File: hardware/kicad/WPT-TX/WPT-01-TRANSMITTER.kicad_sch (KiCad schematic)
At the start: 8 parts, among them J2 Conn_01x12_Pin, J3 Conn_01x05_Pin, J4 Conn_01x04_Pin, J5 12401610E4#2A, SW1 EC11E09244AQ

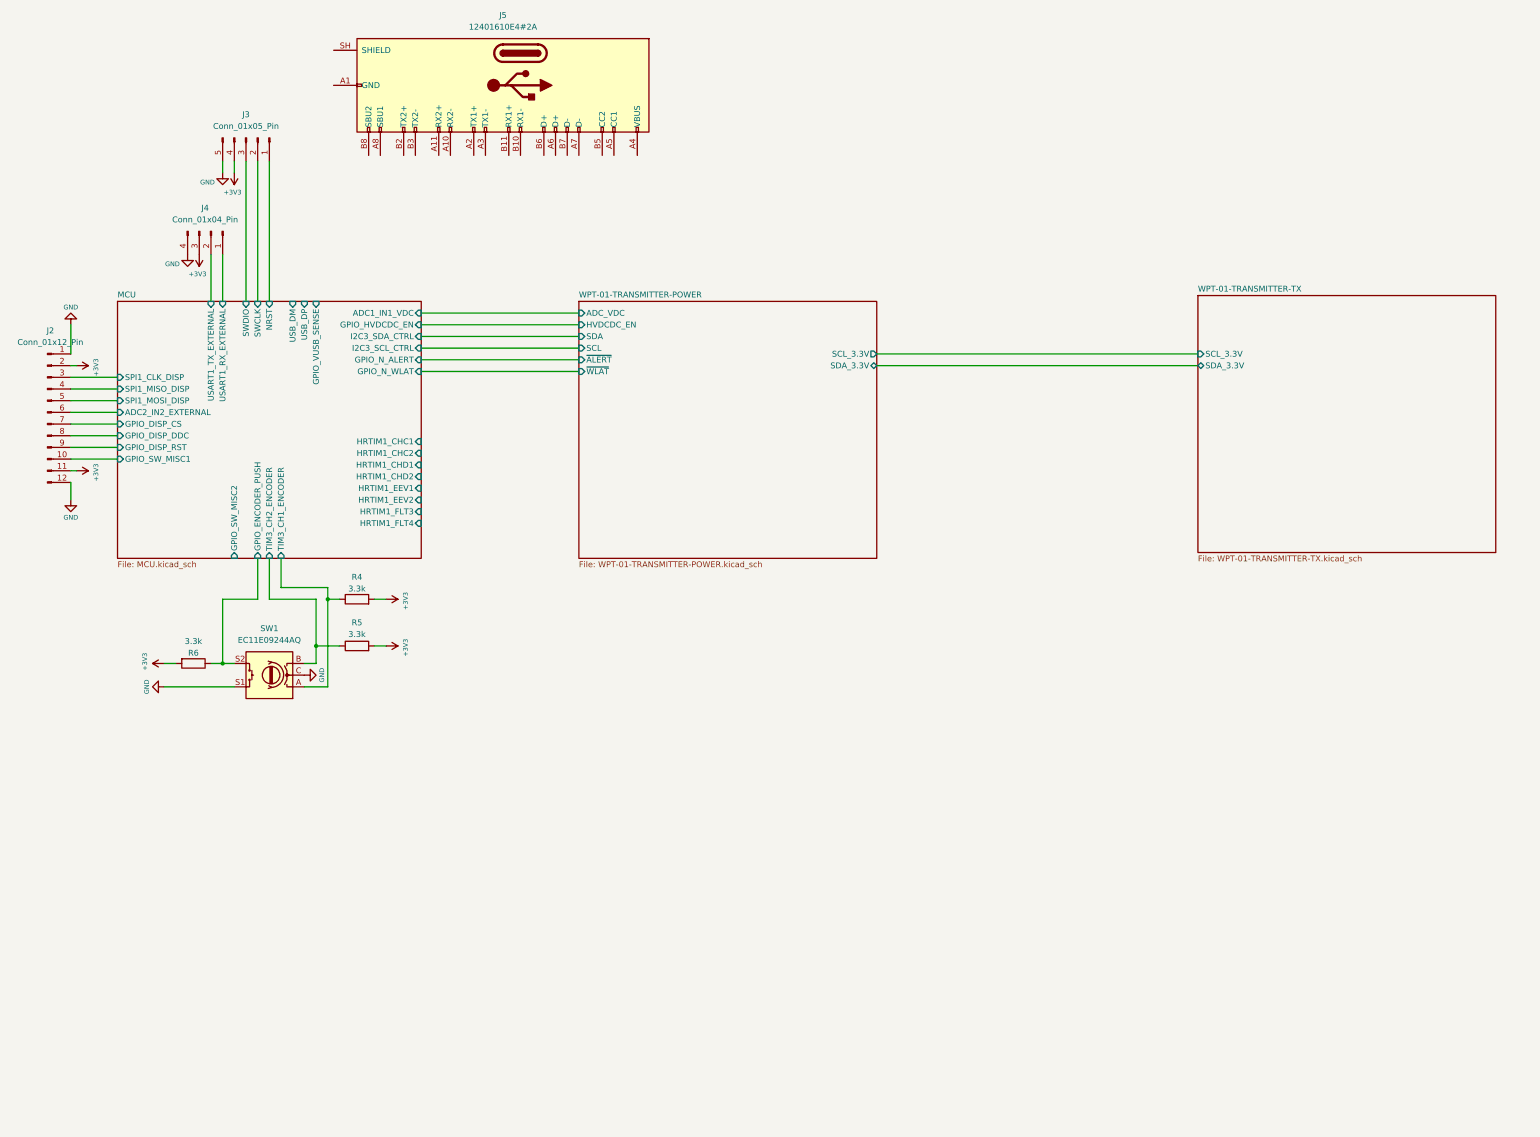
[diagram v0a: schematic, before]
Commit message: add voltage divider for vbus
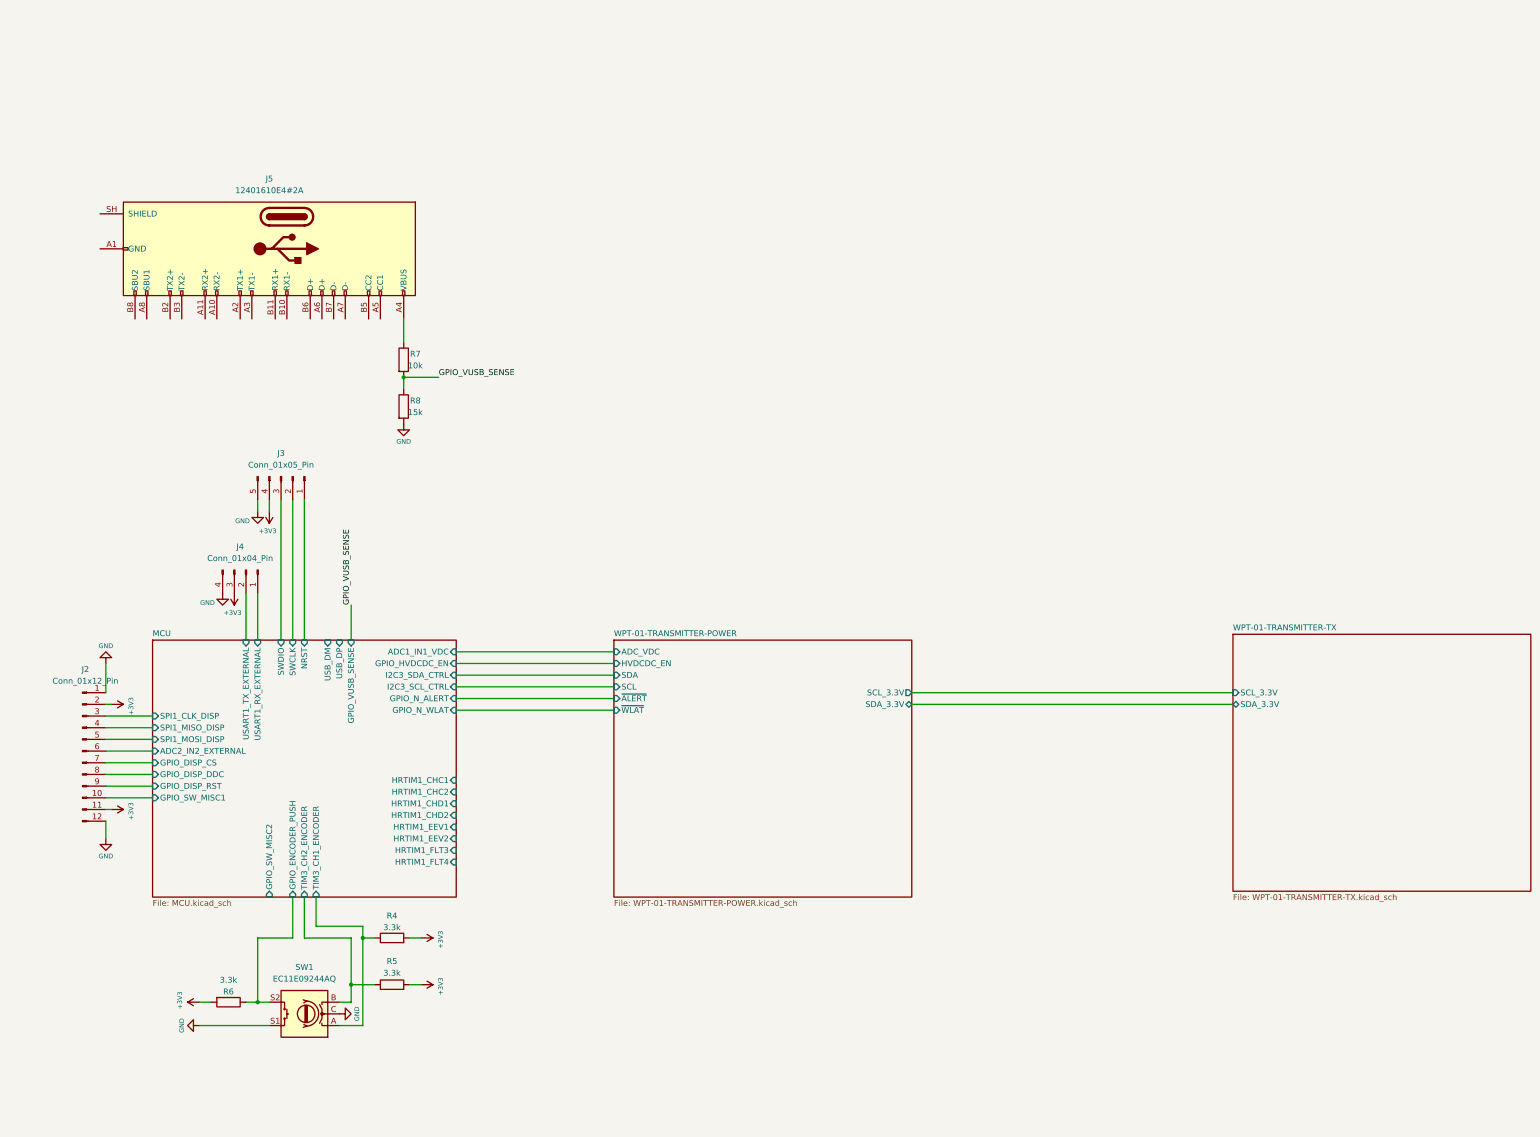
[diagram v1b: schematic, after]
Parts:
- added R7: 10k, Resistor_SMD:R_0402_1005Metric, symbol Device:R
- added R8: 15k, Resistor_SMD:R_0402_1005Metric, symbol Device:R
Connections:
- net GND: now also R8.2
- net at J5.A4 (VBUS), J5.A9 (VBUS), J5.B4 (VBUS)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: now also R7.1
- new net GPIO_VUSB_SENSE: R7.2, R8.1
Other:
- moved on the sheet: J2, J3, J4, J5, R4, R5, R6, SW1

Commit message: USB−C routing
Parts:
- added R10, R9: 5.1k, Resistor_SMD:R_0402_1005Metric, symbol Device:R
- added U3: USBLC6-2SC6, Package_TO_SOT_SMD:SOT-23-6, symbol Power_Protection:USBLC6-2SC6
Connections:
- net GND: now also J5.A1 (GND), J5.A12 (GND), J5.B1 (GND), J5.B12 (GND), J5.SH (SHIELD), R10.2, R9.2, U3.2 (GND)
- net VBUS: now reaches J5.A4 (VBUS), J5.A9 (VBUS), J5.B4 (VBUS), J5.B9 (VBUS), R7.1
- net VBUS: now also U3.5 (VBUS)
- net at J5.A5 (CC1): now also R9.1
- net USB_DP: now reaches J5.A6 (D+)
- net USB_DP: now also J5.B6 (D+), U3.1 (I/O1), U3.6 (I/O1)
- net USB_DM: now reaches J5.A7 (D-)
- net USB_DM: now also J5.B7 (D-), U3.3 (I/O2), U3.4 (I/O2)
- net at J5.B5 (CC2): now also R10.1
- no-connect marks 0 -> 10

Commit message: USB + interlock
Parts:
- added R11: 0, Resistor_SMD:R_0402_1005Metric, symbol Device:R
- added SW2: EG2219, Button_Switch_THT:SW_E-Switch_EG2219_DPDT_Angled, symbol Switch:SW_DPDT_x2
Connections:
- net +3V3: now also SW2.4 (A)
- net GND: now also SW2.6 (C)
- new net HV_EN_MCU: R11.2, SW2.1 (A)
- new net HV_EN_SW: R11.1, SW2.2 (B)
- new net HV_SW_STATE: SW2.5 (B)
- no-connect marks 10 -> 11

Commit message: HRTIM
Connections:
- net MCU/ADC2_IN2_EXTERNAL renamed MCU/ADC2_IN8_EXTERNAL
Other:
- sheet MCU ports: added ADC2_IN8_EXTERNAL, VSWA_CMP, VSWB_CMP; removed ADC2_IN2_EXTERNAL
- sheet WPT-01-TRANSMITTER-TX ports: added HRTIM1_CHC1, HRTIM1_CHC2, HRTIM1_CHD1, HRTIM1_CHD2, HRTIM1_EEV1, HRTIM1_EEV2, HRTIM1_FLT3, HRTIM1_FLT4, VSWA_CMP, VSWB_CMP; removed none
- moved on the sheet: R11, SW2A, SW2B

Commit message: sch: USB4105, standard headers, drop R_LEG
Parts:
- J2: footprint (none) -> Connector_PinHeader_2.54mm:PinHeader_1x12_P2.54mm_Vertical
- J3: footprint (none) -> Connector_PinHeader_2.54mm:PinHeader_1x05_P2.54mm_Vertical
- J4: footprint (none) -> Connector_PinHeader_2.54mm:PinHeader_1x04_P2.54mm_Vertical
- J5: value 12401610E4#2A -> USB4105-GF-A; footprint Connector_USB:USB_C_Receptacle_Amphenol_12401610E4-2A -> Connector_USB:USB_C_Receptacle_GCT_USB4105-xx-A_16P_TopMnt_Horizontal; symbol Connector:USB_C_Receptacle -> Connector:USB_C_Receptacle_USB2.0_16P
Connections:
- no-connect marks 11 -> 3
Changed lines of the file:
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@@
 			)
 		)
-		(property "Footprint" ""
+		(property "Footprint" "Connector_PinHeader_2.54mm:PinHeader_1x05_P2.54mm_Vertical"
 			(at 96.52 111.76 0)
 			(hide yes)
@@
 			)
 		)
-		(property "Footprint" ""
+		(property "Footprint" "Connector_PinHeader_2.54mm:PinHeader_1x04_P2.54mm_Vertical"
 			(at 88.9 132.08 0)
 			(hide yes)
@@
 	)
 	(symbol
-		(lib_id "Connector:USB_C_Receptacle")
-		(at 97.79 62.23 270)
+		(lib_id "Connector:USB_C_Receptacle_USB2.0_16P")
+		(at 107.95 62.23 270)
 		(unit 1)
 		(body_style 1)
@@
 		(in_pos_files yes)
 		(dnp no)
-		(fields_autoplaced yes)
 		(property "Reference" "J5"
-			(at 93.98 46.99 90)
+			(at 107.95 46.99 90)
 			(show_name no)
 			(do_not_autoplace no)
@@
 			)
 		)
-		(property "Value" "12401610E4#2A"
-			(at 93.98 49.53 90)
+		(property "Value" "USB4105-GF-A"
+			(at 107.95 49.53 90)
 			(show_name no)
 			(do_not_autoplace no)
@@
 			)
 		)
-		(property "Footprint" "Connector_USB:USB_C_Receptacle_Amphenol_12401610E4-2A"
-			(at 97.79 66.04 0)
+		(property "Footprint" "Connector_USB:USB_C_Receptacle_GCT_USB4105-xx-A_16P_TopMnt_Horizontal"
+			(at 107.95 62.23 0)
 			(hide yes)
 			(show_name no)
@@
 			)
 		)
-		(property "Datasheet" "https://www.usb.org/sites/default/files/documents/usb_type-c.zip"
-			(at 97.79 66.04 0)
+		(property "Datasheet" "https://gct.co/files/drawings/usb4105.pdf"
+			(at 107.95 62.23 0)
 			(hide yes)
 			(show_name no)
@@
 			)
 		)
-		(property "Description" "USB Full-Featured Type-C Receptacle connector"
-			(at 97.79 62.23 0)
+		(property "Description" "USB 2.0-only Type-C Receptacle connector, 16 pin (GCT USB4105)"
+			(at 107.95 62.23 0)
 			(hide yes)
 			(show_name no)
@@
 			)
 		)
-		(pin "A12"
-		)
-		(pin "B1"
+		(pin "A1"
 		)
-		(pin "B2"
+		(pin "A4"
 		)
-		(pin "A10"
+		(pin "A5"
 		)
-		(pin "A11"
+		(pin "A6"
 		)
 		(pin "A7"
@@
 		(pin "A9"
 		)
-		(pin "A1"
-		)
-		(pin "A2"
-		)
-		(pin "A3"
-		)
-		(pin "A4"
-		)
-		(pin "A5"
-		)
-		(pin "A6"
+		(pin "A12"
 		)
-		(pin "B3"
+		(pin "B1"
 		)
 		(pin "B4"
@@
 		(pin "B9"
 		)
-		(pin "B10"
-		)
-		(pin "B11"
-		)
 		(pin "B12"
 		)
@@
 			)
 		)
-		(property "Footprint" ""
+		(property "Footprint" "Connector_PinHeader_2.54mm:PinHeader_1x12_P2.54mm_Vertical"
 			(at 53.34 171.45 0)
 			(hide yes)
@@
 		)
 	)
-	(wire
-		(pts
-			(xy 57.15 62.23) (xy 53.34 62.23)
-		)
-		(stroke
-			(width 0)
-			(type default)
-		)
-	)
-	(wire
-		(pts
-			(xy 53.34 62.23) (xy 53.34 64.77)
-		)
-		(stroke
-			(width 0)
-			(type default)
-		)
-	)
-	(wire
-		(pts
-			(xy 57.15 54.61) (xy 50.8 54.61)
-		)
-		(stroke
-			(width 0)
-			(type default)
-		)
-	)
-	(wire
-		(pts
-			(xy 50.8 54.61) (xy 50.8 64.77)
-		)
-		(stroke
-			(width 0)
-			(type default)
-		)
-	)
-	(wire
-		(pts
-			(xy 50.8 64.77) (xy 53.34 64.77)
-		)
-		(stroke
-			(width 0)
-			(type default)
-		)
-	)
-	(junction
-		(at 53.34 64.77)
-		(diameter 0)
-		(color 0 0 0 0)
-	)
 	(symbol
 		(lib_id "power:GND")
-		(at 53.34 64.77 0)
+		(at 82.55 64.77 0)
 		(unit 1)
 		(body_style 1)
@@
 		)
 		(property "Value" "GND"
-			(at 53.34 68.58 0)
+			(at 82.55 68.58 0)
 			(show_name no)
 			(do_not_autoplace no)
@@
 		)
 		(property "Footprint" ""
-			(at 53.34 64.77 0)
+			(at 82.55 64.77 0)
 			(hide yes)
 			(show_name no)
@@
 		)
 		(property "Datasheet" ""
-			(at 53.34 64.77 0)
+			(at 82.55 64.77 0)
 			(hide yes)
 			(show_name no)
@@
 		)
 		(property "Description" ""
-			(at 53.34 64.77 0)
+			(at 82.55 64.77 0)
 			(show_name no)
 			(do_not_autoplace no)
@@
 	)
 	(no_connect
-		(at 64.77 77.47)
-	)
-	(no_connect
-		(at 67.31 77.47)
-	)
-	(no_connect
-		(at 72.39 77.47)
-	)
-	(no_connect
-		(at 74.93 77.47)
-	)
-	(no_connect
-		(at 80.01 77.47)
-	)
-	(no_connect
-		(at 82.55 77.47)
-	)
-	(no_connect
-		(at 87.63 77.47)
-	)
-	(no_connect
-		(at 90.17 77.47)
-	)
-	(no_connect
 		(at 95.25 77.47)
 	)
-	(no_connect
-		(at 97.79 77.47)
-	)
 	(symbol
 		(lib_id "Power_Protection:USBLC6-2SC6")
@@
 		)
 	)
+	(wire
+		(pts
+			(xy 85.09 62.23) (xy 82.55 62.23)
+		)
+		(stroke
+			(width 0)
+			(type default)
+		)
+	)
+	(wire
+		(pts
+			(xy 82.55 62.23) (xy 82.55 64.77)
+		)
+		(stroke
+			(width 0)
+			(type default)
+		)
+	)
+	(wire
+		(pts
+			(xy 85.09 54.61) (xy 80.01 54.61)
+		)
+		(stroke
+			(width 0)
+			(type default)
+		)
+	)
+	(wire
+		(pts
+			(xy 80.01 54.61) (xy 80.01 64.77)
+		)
+		(stroke
+			(width 0)
+			(type default)
+		)
+	)
+	(wire
+		(pts
+			(xy 80.01 64.77) (xy 82.55 64.77)
+		)
+		(stroke
+			(width 0)
+			(type default)
+		)
+	)
+	(junction
+		(at 82.55 64.77)
+		(diameter 0)
+		(color 0 0 0 0)
+	)
+	(no_connect
+		(at 92.71 77.47)
+	)
 	(sheet_instances
